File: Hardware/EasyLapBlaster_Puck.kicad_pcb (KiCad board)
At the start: 2 copper layers, 30.5 x 114.3 mm, 34 parts, among them IC1 PIC10F322, P2 CONN_01X06, Q1 AO3401A, Q2 AO3400A, SW1 SPST, U1 HS0038B, U2 DW-01, U3 FS8205

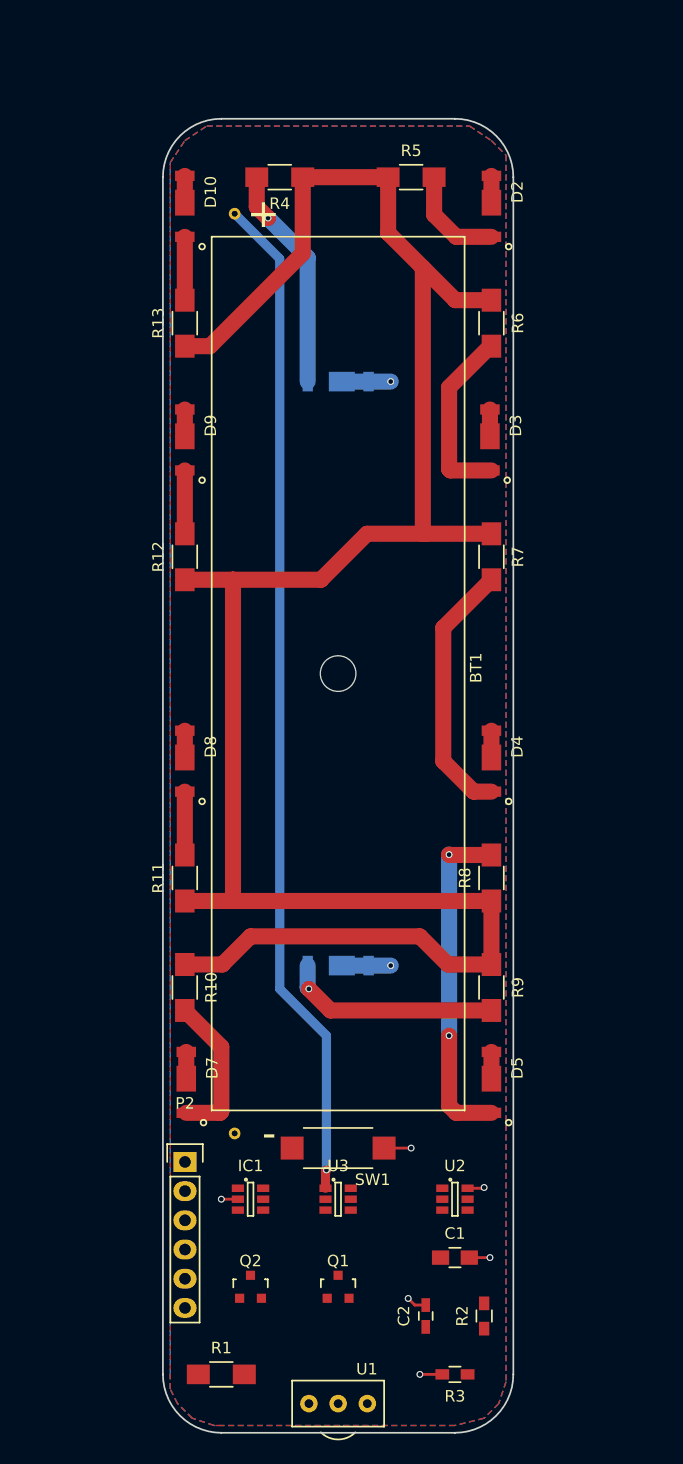
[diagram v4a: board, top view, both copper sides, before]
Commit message: Widened board slightly and finished traces.
Widened board by about 4mm to allow Vbat zone to reach all of the LED's.
Finished all traces.  Ready for QC
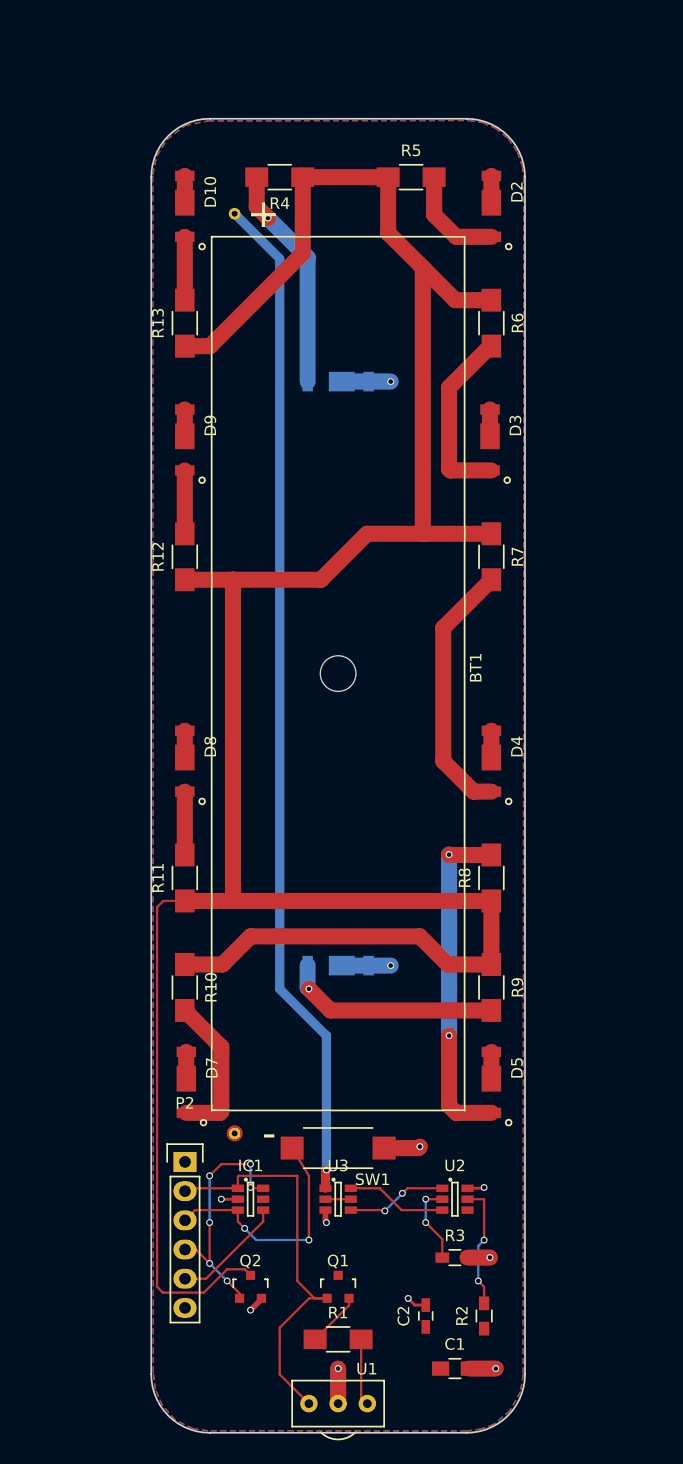
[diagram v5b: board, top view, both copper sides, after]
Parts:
- moved R1 10.6 mm to (147.3, 154.4)
- moved R3 10.2 mm to (157.5, 147.3), turned to 0 degrees
- moved C1 9.65 mm to (157.5, 157.0)
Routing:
- net Net-(Q2-Pad3): track 184.6 -> 229.7 mm
- net /RA0: track 0.00 -> 36.2 mm
- net /RA2: track 0.00 -> 21.5 mm, vias 0 -> 6
- net /RA1: track 0.00 -> 21.2 mm, vias 0 -> 2
- net Net-(R2-Pad2): track 0.00 -> 10.9 mm, vias 0 -> 2
- net /RA3: track 0.00 -> 9.86 mm
- net /G1: track 0.00 -> 8.80 mm, vias 0 -> 2
- net /G2: track 0.00 -> 8.75 mm
- net Net-(R3-Pad1): track 0.00 -> 7.12 mm, vias 0 -> 2
- net /GND: track 10.8 -> 17.7 mm, vias 6 -> 9
- net Net-(R1-Pad2): track 0.00 -> 5.81 mm
- net Net-(Q1-Pad2): track 0.00 -> 4.79 mm
- net /D12: track 0.00 -> 2.20 mm
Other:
- board size 30.5 x 114.3 mm -> 32.5 x 114.3 mm
- net class Data Line added: clearance 0.2, trace_width 0.2, via_dia 0.6, via_drill 0.4
- net class Ground added: clearance 0, trace_width 0.5, via_dia 0.6, via_drill 0.4
